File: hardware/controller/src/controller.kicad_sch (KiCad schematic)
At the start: 31 parts, among them J1 To Display, J2 Display, J3 Barrel_Jack_Switch, J4 Program, J5 JTAG, SW1 RESET, SW2 BTN1, SW3 BTN1, U1 ESP32-WROOM-32D, U2 XL1509-5.0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

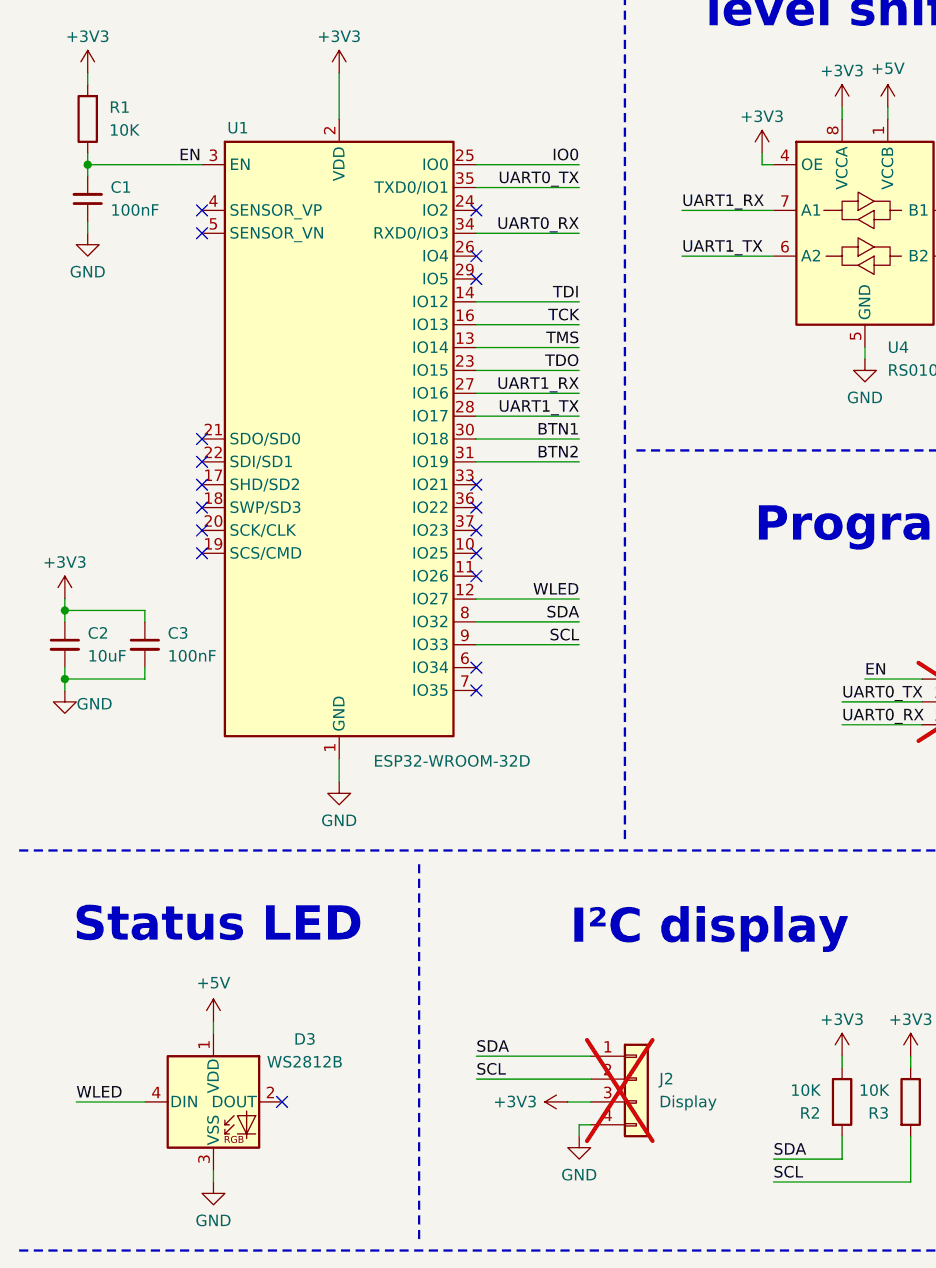
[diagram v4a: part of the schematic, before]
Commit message: Added some testpads
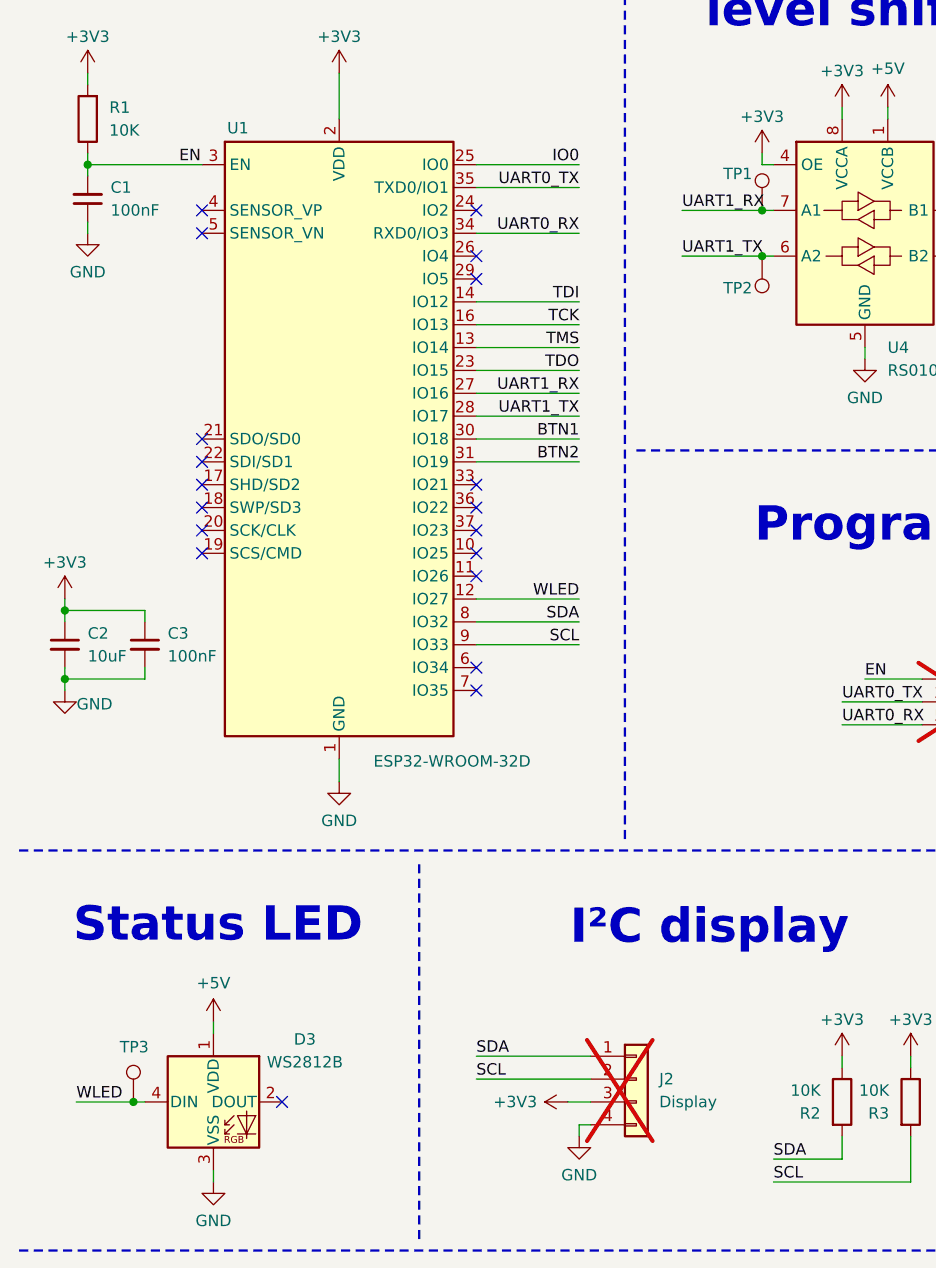
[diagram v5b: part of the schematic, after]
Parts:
- added TP1, TP2, TP3: ~, TestPoint:TestPoint_Pad_D1.5mm, symbol Connector:TestPoint
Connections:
- net UART1_RX: now also TP1.1
- net UART1_TX: now also TP2.1
- net WLED: now also TP3.1

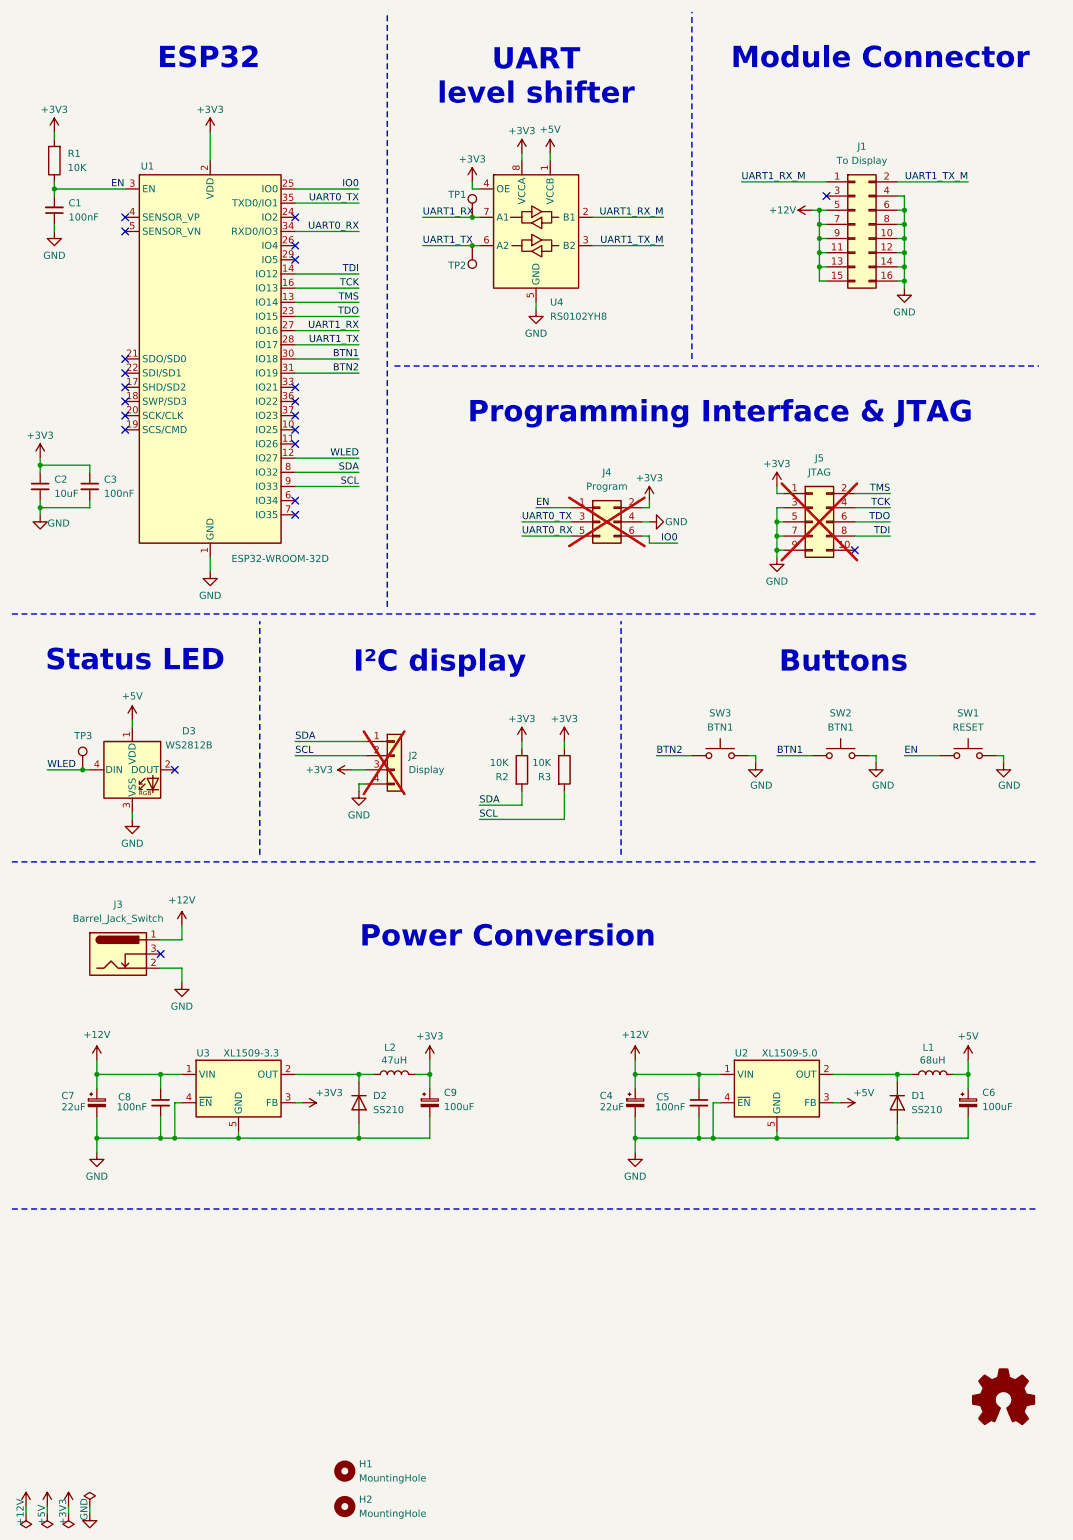
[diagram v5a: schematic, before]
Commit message: added blender renderes to kibot
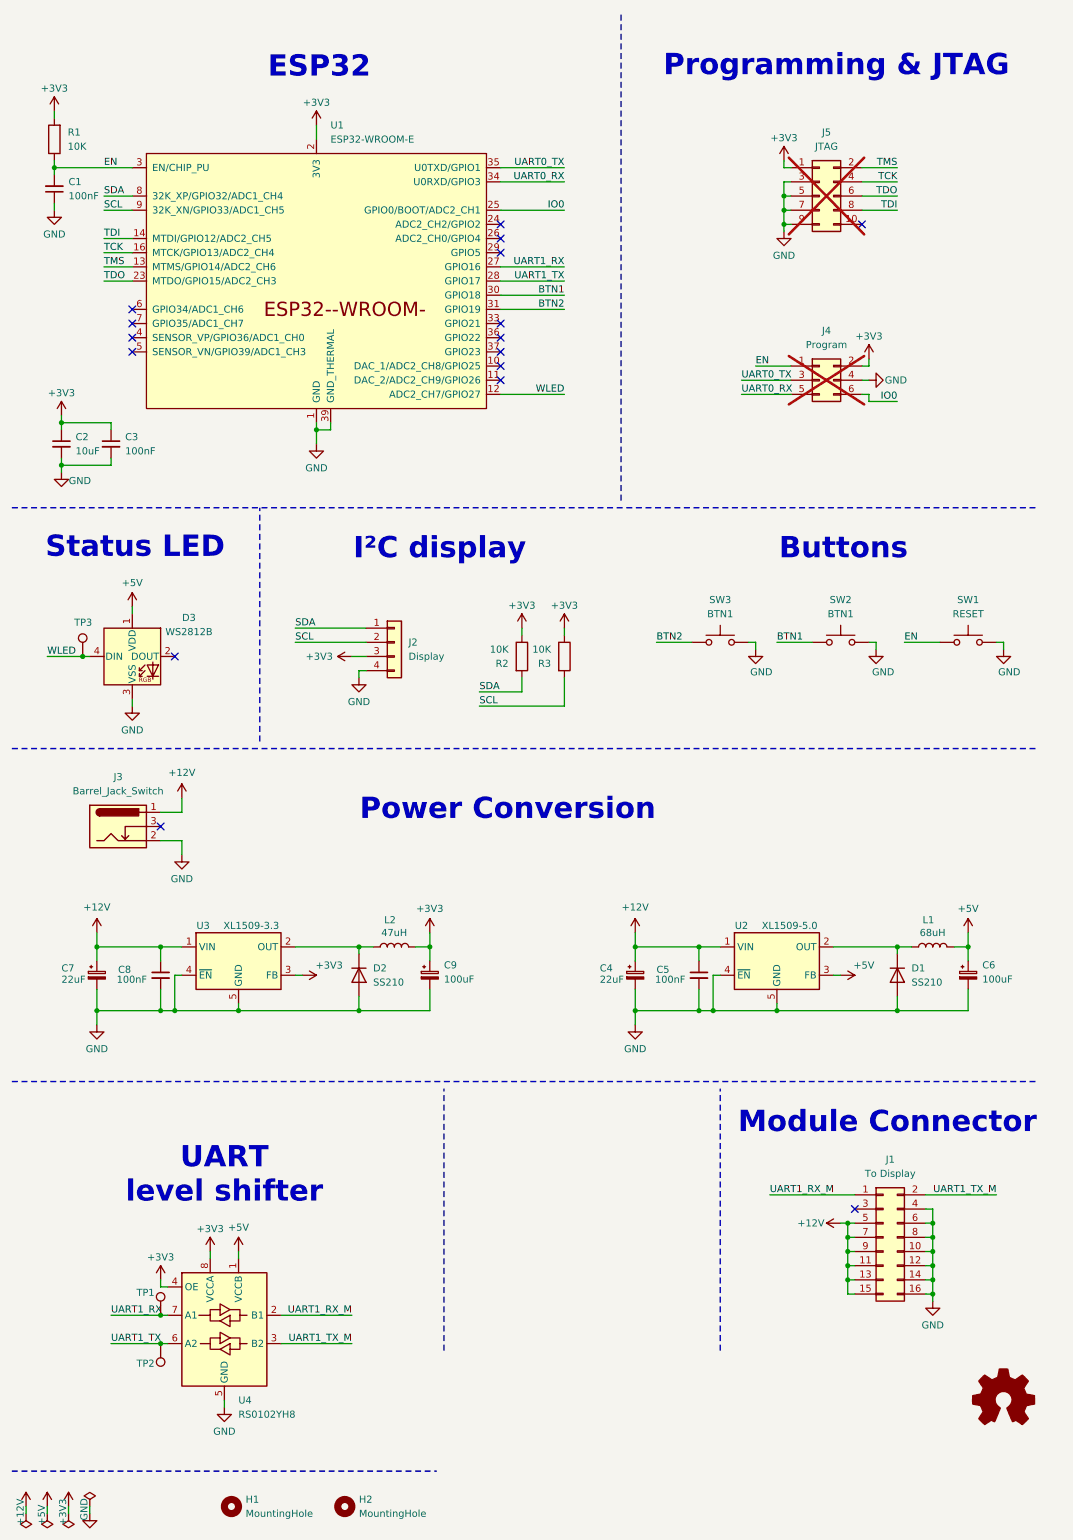
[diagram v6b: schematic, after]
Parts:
- removed U1: ESP32-WROOM-32D, RF_Module:ESP32-WROOM-32D, symbol RF_Module:ESP32-WROOM-32D
- added U1: ESP32-WROOM-E, PCM_Espressif:ESP32-WROOM-32E, symbol PCM_Espressif:ESP32-WROOM-E
- J2: now fitted
- SW1, SW2, SW3: footprint Button_Switch_SMD:SW_Push_1P1T_NO_6x6mm_H9.5mm -> Button_Switch_SMD:SW_SPST_PTS645
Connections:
- net +3V3: now also U1.2 (3V3)
- net BTN1: now also U1.30 (GPIO18)
- net BTN2: now also U1.31 (GPIO19)
- net EN: now also U1.3 (EN/CHIP_PU)
- net GND: now also U1.1 (GND), U1.15 (GND), U1.38 (GND), U1.39 (GND_THERMAL)
- net IO0: now also U1.25 (GPIO0/BOOT/ADC2_CH1)
- net SCL: now also U1.9 (32K_XN/GPIO33/ADC1_CH5)
- net SDA: now also U1.8 (32K_XP/GPIO32/ADC1_CH4)
- net TCK: now also U1.16 (MTCK/GPIO13/ADC2_CH4)
- net TDI: now also U1.14 (MTDI/GPIO12/ADC2_CH5)
- net TDO: now also U1.23 (MTDO/GPIO15/ADC2_CH3)
- net TMS: now also U1.13 (MTMS/GPIO14/ADC2_CH6)
- net UART0_RX: now also U1.34 (U0RXD/GPIO3)
- net UART0_TX: now also U1.35 (U0TXD/GPIO1)
- net UART1_RX: now also U1.27 (GPIO16)
- net UART1_TX: now also U1.28 (GPIO17)
- net WLED: now also U1.12 (ADC2_CH7/GPIO27)
- no-connect marks 22 -> 16
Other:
- note added: "Programming & JTAG"
- note removed: "Programming Interface & JTAG"
- moved on the sheet: C1, C2, C3, C4, C5, C6, C7, C8, C9, D1, D2, D3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

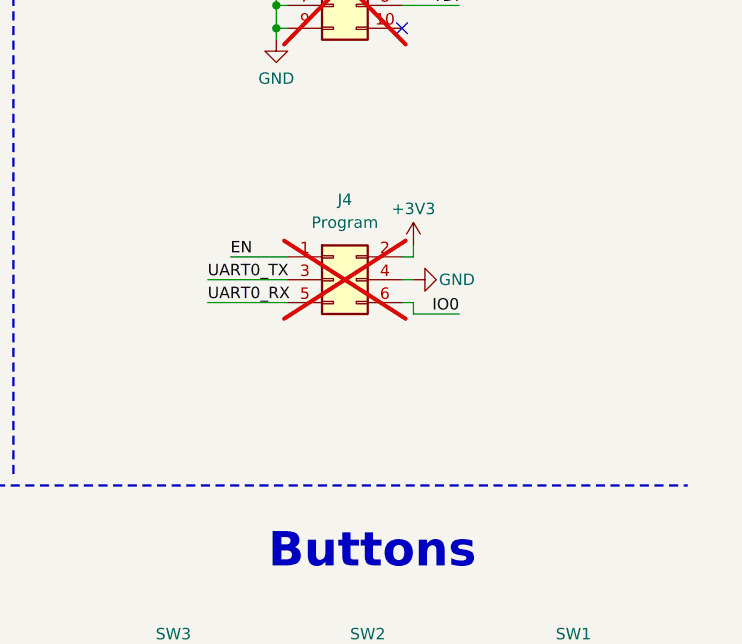
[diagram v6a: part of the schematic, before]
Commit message: Updated controller footprint and added testpads
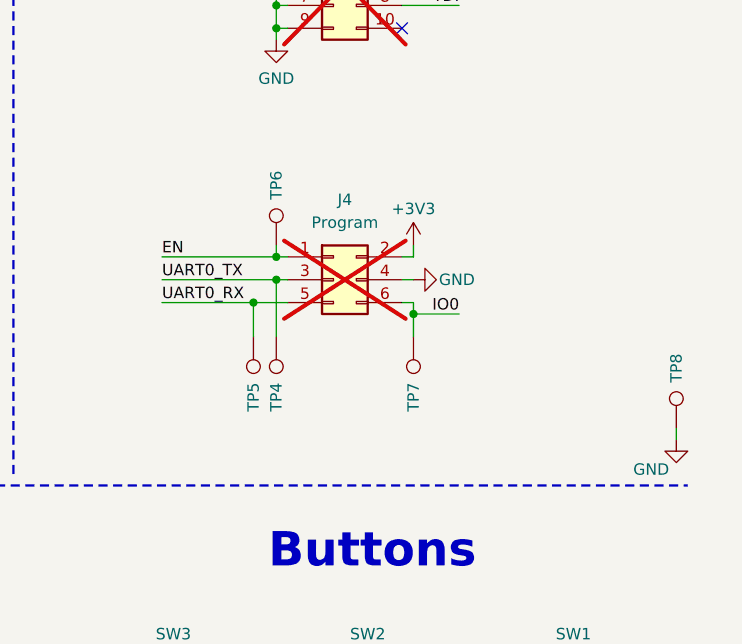
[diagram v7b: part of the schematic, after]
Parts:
- added TP4, TP5, TP6, TP7, TP8: ~, TestPoint:TestPoint_Pad_D1.5mm, symbol Connector:TestPoint
- U4: footprint Package_SO:TSSOP-8_3x3mm_P0.65mm -> Package_TO_SOT_SMD:SOT-23-8
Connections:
- net EN: now also TP6.1
- net GND: now also TP8.1
- net IO0: now also TP7.1
- net UART0_RX: now also TP5.1
- net UART0_TX: now also TP4.1

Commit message: Added LCSC part number for esp32
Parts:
- U1: LCSC (none) -> C701343
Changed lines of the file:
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@@
+			)
+		)
+		(property "LCSC" "C701343"
+			(at 67.31 60.96 0)
+			(effects
+				(font
+					(size 1.27 1.27)
+				)
+				(hide yes)
 			)
 		)
